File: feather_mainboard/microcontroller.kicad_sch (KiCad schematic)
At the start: 3 parts, among them U1 Adafruit ESP32-S3 Feather

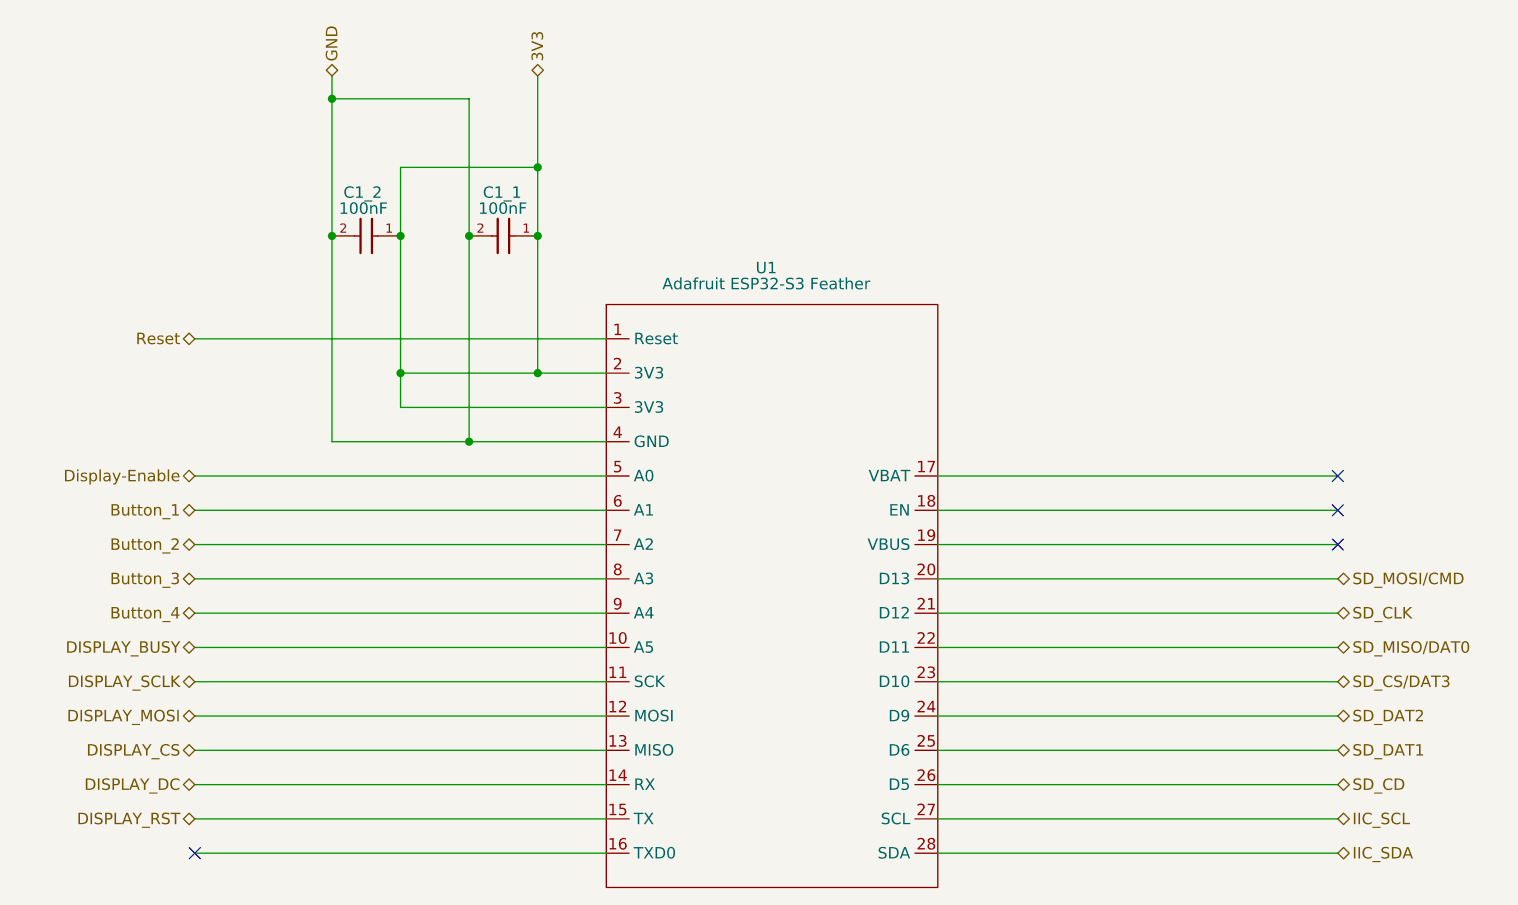
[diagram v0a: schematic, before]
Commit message: Updated the mainboard: removed unnecessary pull-ups on SD card lines; connected IIC pull-ups to enable circuit; cleaned up schematic
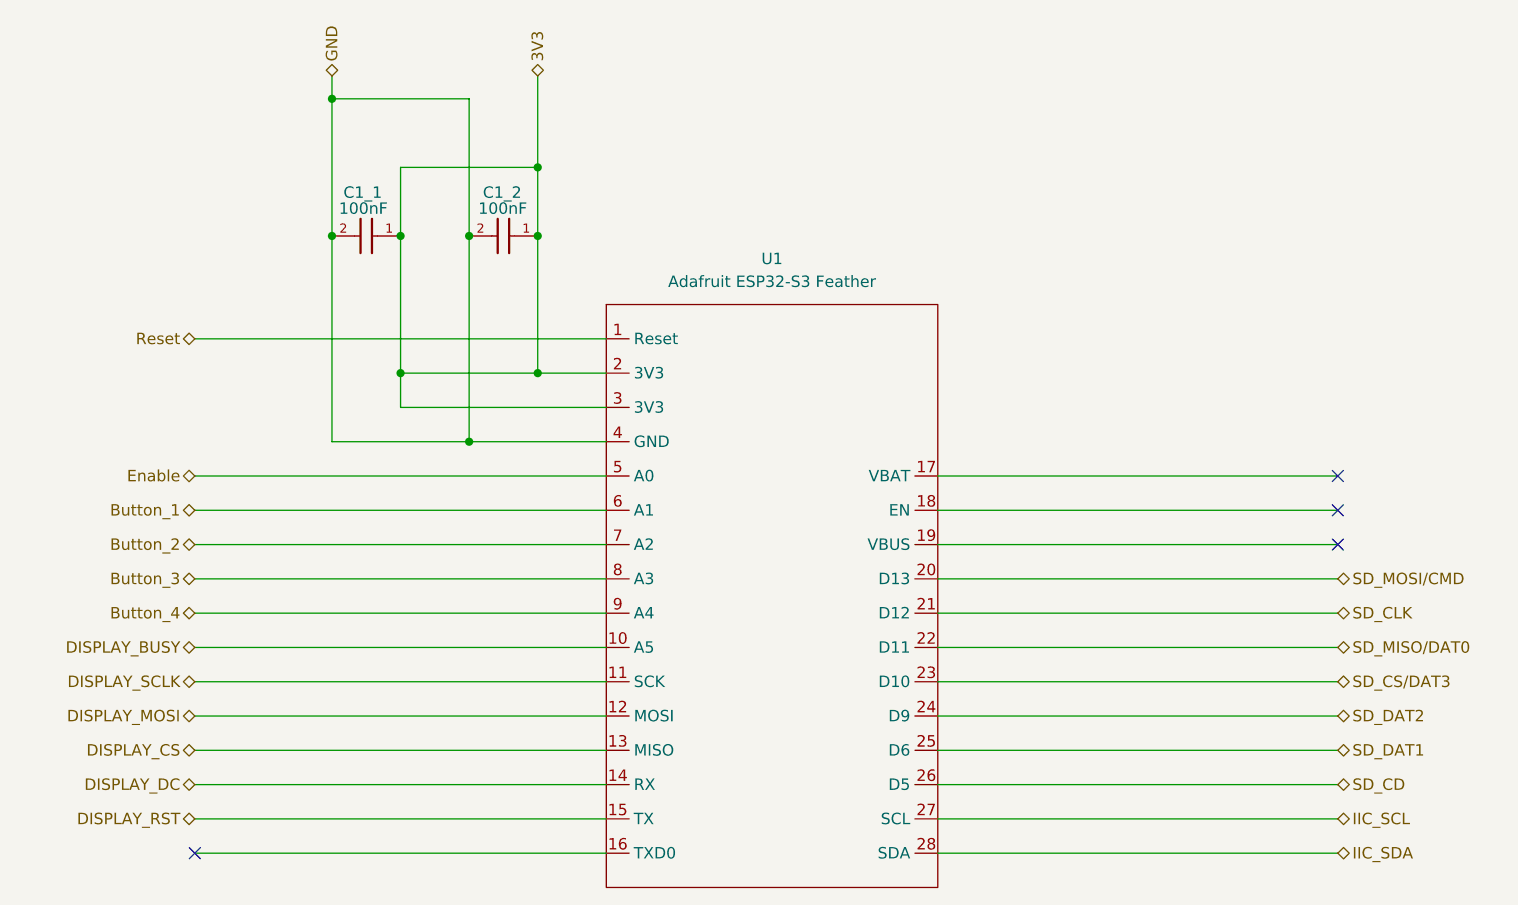
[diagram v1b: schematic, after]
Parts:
- renumbered C1_2 to C1_1, C1_1 to C1_2
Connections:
- net Display-Enable renamed Enable
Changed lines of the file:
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@@
 		)
 	)
-	(hierarchical_label "Display-Enable"
+	(hierarchical_label "Enable"
 		(shape bidirectional)
 		(at 95.25 82.55 180)
+		(fields_autoplaced yes)
 		(effects
 			(font
@@
 		(shape bidirectional)
 		(at 222.25 116.84 0)
+		(fields_autoplaced yes)
 		(effects
 			(font
@@
 		(shape bidirectional)
 		(at 222.25 113.03 0)
+		(fields_autoplaced yes)
 		(effects
 			(font
@@
 		(shape bidirectional)
 		(at 222.25 93.98 0)
+		(fields_autoplaced yes)
 		(effects
 			(font
@@
 		(shape bidirectional)
 		(at 222.25 105.41 0)
+		(fields_autoplaced yes)
 		(effects
 			(font
@@
 		(shape bidirectional)
 		(at 95.25 120.65 180)
+		(fields_autoplaced yes)
 		(effects
 			(font
@@
 		(shape bidirectional)
 		(at 95.25 67.31 180)
+		(fields_autoplaced yes)
 		(effects
 			(font
@@
 		(shape bidirectional)
 		(at 110.49 38.1 90)
+		(fields_autoplaced yes)
 		(effects
 			(font
@@
 		(shape bidirectional)
 		(at 95.25 113.03 180)
+		(fields_autoplaced yes)
 		(effects
 			(font
@@
 		(shape bidirectional)
 		(at 222.25 120.65 0)
+		(fields_autoplaced yes)
 		(effects
 			(font
@@
 		(shape bidirectional)
 		(at 222.25 101.6 0)
+		(fields_autoplaced yes)
 		(effects
 			(font
@@
 		(shape bidirectional)
 		(at 222.25 97.79 0)
+		(fields_autoplaced yes)
 		(effects
 			(font
@@
 		(shape bidirectional)
 		(at 133.35 38.1 90)
+		(fields_autoplaced yes)
 		(effects
 			(font
@@
 		(shape bidirectional)
 		(at 95.25 97.79 180)
+		(fields_autoplaced yes)
 		(effects
 			(font
@@
 		(shape bidirectional)
 		(at 222.25 109.22 0)
+		(fields_autoplaced yes)
 		(effects
 			(font
@@
 		(shape bidirectional)
 		(at 95.25 93.98 180)
+		(fields_autoplaced yes)
 		(effects
 			(font
@@
 		(shape bidirectional)
 		(at 95.25 101.6 180)
+		(fields_autoplaced yes)
 		(effects
 			(font
@@
 		(shape bidirectional)
 		(at 95.25 90.17 180)
+		(fields_autoplaced yes)
 		(effects
 			(font
@@
 		(shape bidirectional)
 		(at 95.25 109.22 180)
+		(fields_autoplaced yes)
 		(effects
 			(font
@@
 		(shape bidirectional)
 		(at 95.25 105.41 180)
+		(fields_autoplaced yes)
 		(effects
 			(font
@@
 		(shape bidirectional)
 		(at 222.25 124.46 0)
+		(fields_autoplaced yes)
 		(effects
 			(font
@@
 		(shape bidirectional)
 		(at 95.25 86.36 180)
+		(fields_autoplaced yes)
 		(effects
 			(font
@@
 		(shape bidirectional)
 		(at 95.25 116.84 180)
+		(fields_autoplaced yes)
 		(effects
 			(font
@@
 		(fields_autoplaced yes)
 		(property "Reference" "U1"
-			(at 158.75 59.436 0)
+			(at 159.385 58.42 0)
 			(effects
 				(font
@@
 		)
 		(property "Value" "Adafruit ESP32-S3 Feather"
-			(at 158.75 61.214 0)
+			(at 159.385 60.96 0)
 			(effects
 				(font
@@
 		(instances
 			(project "feather_mainboard"
-				(path "/e1e12730-ab4f-45db-8b66-c1e0f78e2f00/2e3e5636-c492-45ef-bece-a2815296f467"
+				(path "/e1e12730-ab4f-45db-8b66-c1e0f78e2f00/98c01520-deea-4d79-9e46-95cc0e470bab"
 					(reference "U1")
 					(unit 1)
@@
 		(on_board yes)
 		(dnp no)
-		(property "Reference" "C1_2"
+		(property "Reference" "C1_1"
 			(at 111.76 51.054 0)
 			(effects
@@
 		(instances
 			(project "feather_mainboard"
-				(path "/e1e12730-ab4f-45db-8b66-c1e0f78e2f00/2e3e5636-c492-45ef-bece-a2815296f467"
-					(reference "C1_2")
+				(path "/e1e12730-ab4f-45db-8b66-c1e0f78e2f00/98c01520-deea-4d79-9e46-95cc0e470bab"
+					(reference "C1_1")
 					(unit 1)
 				)
@@
 		(on_board yes)
 		(dnp no)
-		(property "Reference" "C1_1"
+		(property "Reference" "C1_2"
 			(at 127.254 51.054 0)
 			(effects
@@
 		(instances
 			(project "feather_mainboard"
-				(path "/e1e12730-ab4f-45db-8b66-c1e0f78e2f00/2e3e5636-c492-45ef-bece-a2815296f467"
-					(reference "C1_1")
+				(path "/e1e12730-ab4f-45db-8b66-c1e0f78e2f00/98c01520-deea-4d79-9e46-95cc0e470bab"
+					(reference "C1_2")
 					(unit 1)
 				)
